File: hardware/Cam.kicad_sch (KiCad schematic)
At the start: 1 part

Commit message: feat(Hw):Update_Schematic_And_BOM
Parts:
- removed Cam1: F31L-1A7H1-11024, Connector_FFC-FPC:Hirose_FH12-24S-0.5SH_1x24-1MP_P0.50mm_Horizontal, symbol F31L-1A7H1-11024:F31L-1A7H1-11024
- added J1: Conn_01x20, Connector_FFC-FPC:Hirose_FH12-20S-0.5SH_1x20-1MP_P0.50mm_Horizontal, symbol Connector_Generic:Conn_01x20
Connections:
- net +3V3: now also J1.19 (Pin_19), J1.20 (Pin_20)
- net CSI_SCK: now also J1.13 (Pin_13)
- net CSI_SDA: now also J1.14 (Pin_14)
- net GND: now also J1.1 (Pin_1), J1.12 (Pin_12), J1.15 (Pin_15), J1.17 (Pin_17), J1.18 (Pin_18), J1.3 (Pin_3), J1.6 (Pin_6), J1.9 (Pin_9)
- net MCSI_CKN: now also J1.8 (Pin_8)
- net MCSI_CKP: now also J1.7 (Pin_7)
- net MCSI_D0N: now also J1.5 (Pin_5)
- net MCSI_D0P: now also J1.4 (Pin_4)
- net MCSI_D1N: now also J1.11 (Pin_11)
- net MCSI_D1P: now also J1.10 (Pin_10)
- net MCSI_MCLK: now also J1.2 (Pin_2)
- net MCSI_RST: now also J1.16 (Pin_16)

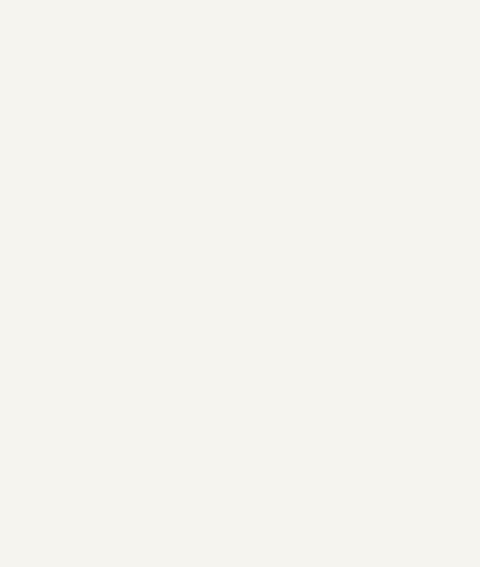
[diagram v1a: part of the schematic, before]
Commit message: feat(Hw):Update_Schematic_And_Floorplan
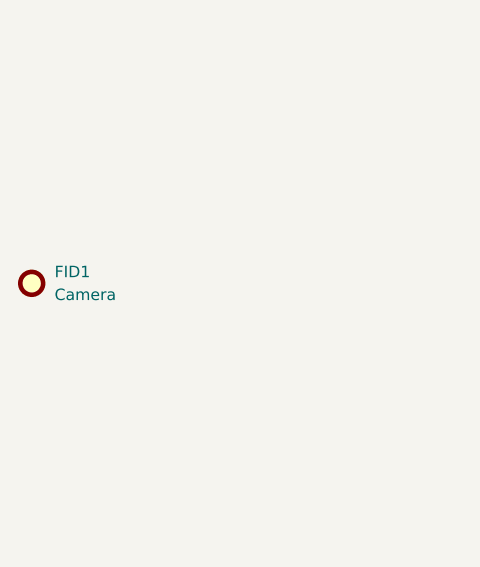
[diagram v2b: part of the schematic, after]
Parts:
- added FID1: Camera, Footprints:Camera, symbol Mechanical:Fiducial
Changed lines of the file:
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@@
+		)
+	)
+	(symbol
+		(lib_id "Mechanical:Fiducial")
+		(at 53.34 54.61 0)
+		(unit 1)
+		(exclude_from_sim no)
+		(in_bom no)
+		(on_board yes)
+		(dnp no)
+		(fields_autoplaced yes)
+		(property "Reference" "FID1"
+			(at 55.88 53.3399 0)
+			(effects
+				(font
+					(size 1.27 1.27)
+				)
+				(justify left)
+			)
+		)
+		(property "Value" "Camera"
+			(at 55.88 55.8799 0)
+			(effects
+				(font
+					(size 1.27 1.27)
+				)
+				(justify left)
+			)
+		)
+		(property "Footprint" "Footprints:Camera"
+			(at 53.34 54.61 0)
+			(effects
+				(font
+					(size 1.27 1.27)
+				)
+				(hide yes)
+			)
+		)
+		(property "Datasheet" "~"
+			(at 53.34 54.61 0)
+			(effects
+				(font
+					(size 1.27 1.27)
+				)
+				(hide yes)
+			)
+		)
+		(property "Description" "Fiducial Marker"
+			(at 53.34 54.61 0)
+			(effects
+				(font
+					(size 1.27 1.27)
+				)
+				(hide yes)
+			)
+		)
+		(property "manf#" "https://www.luckfox.com/EN-SC3336-3MP-Camera-B"
+			(at 53.34 54.61 0)
+			(effects
+				(font
+					(size 1.27 1.27)
+				)
+				(hide yes)
+			)
+		)
+		(instances
+			(project ""
+				(path "/aee06ce3-1da5-4230-bf8f-9d1068f7ddd5/81efd129-08c1-4996-9ee0-a58d47ad59bf"
+					(reference "FID1")
+					(unit 1)
+				)
+			)
 		)
 	)

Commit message: feat(Hw):Update_Schematic_And_Floorplan
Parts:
- FID1: footprint Footprints:Camera -> Footprints:Untitled
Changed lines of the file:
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@@
 			)
 		)
-		(property "Footprint" "Footprints:Camera"
+		(property "Footprint" "Footprints:Untitled"
 			(at 53.34 54.61 0)
 			(effects

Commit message: feat(Hw):Update_Route
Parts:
- added J3: FLEX_TO_CAM, symbol Connector:Conn_01x01_Pin
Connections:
- no-connect marks 0 -> 1
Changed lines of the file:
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@@
 		(color 0 0 0 0)
+	)
+	(no_connect
+		(at 58.42 67.31)
 	)
 	(wire
@@
 					(unit 1)
 				)
+			)
+		)
+	)
+	(symbol
+		(lib_id "Connector:Conn_01x01_Pin")
+		(at 53.34 67.31 0)
+		(unit 1)
+		(exclude_from_sim no)
+		(in_bom yes)
+		(on_board yes)
+		(dnp no)
+		(fields_autoplaced yes)
+		(property "Reference" "J3"
+			(at 53.975 62.23 0)
+			(effects
+				(font
+					(size 1.27 1.27)
+				)
+			)
+		)
+		(property "Value" "FLEX_TO_CAM"
+			(at 53.975 64.77 0)
+			(effects
+				(font
+					(size 1.27 1.27)
+				)
+			)
+		)
+		(property "Footprint" ""
+			(at 53.34 67.31 0)
+			(effects
+				(font
+					(size 1.27 1.27)
+				)
+				(hide yes)
+			)
+		)
+		(property "Datasheet" "~"
+			(at 53.34 67.31 0)
+			(effects
+				(font
+					(size 1.27 1.27)
+				)
+				(hide yes)
+			)
+		)
+		(property "Description" "Generic connector, single row, 01x01, script generated"
+			(at 53.34 67.31 0)
+			(effects
+				(font
+					(size 1.27 1.27)
+				)
+				(hide yes)
+			)
+		)
+		(property "LCSC#" "C22434842"
+			(at 53.34 67.31 0)
+			(effects
+				(font
+					(size 1.27 1.27)
+				)
+				(hide yes)
+			)
+		)
+		(pin "1"
+		)
+		(instances
+			(project "Badge-HackGDL-2026"
+				(path "/aee06ce3-1da5-4230-bf8f-9d1068f7ddd5/81efd129-08c1-4996-9ee0-a58d47ad59bf"
+					(reference "J3")
+					(unit 1)
+				)

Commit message: feat(Hw):Update_Schematic_And_Route
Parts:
- renumbered FID1 to FID?, J1 to J?, J3 to J?
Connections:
- net +3V3: now also J?.1 (Pin_1), J?.2 (Pin_2); no longer J?.19 (Pin_19), J?.20 (Pin_20)
- net CSI_SCK: now also J?.8 (Pin_8); no longer J?.13 (Pin_13)
- net CSI_SDA: now also J?.7 (Pin_7); no longer J?.14 (Pin_14)
- net GND: now also J?.20 (Pin_20), J?.4 (Pin_4); no longer J?.1 (Pin_1), J?.17 (Pin_17)
- net MCSI_CKN: now also J?.13 (Pin_13); no longer J?.8 (Pin_8)
- net MCSI_CKP: now also J?.14 (Pin_14); no longer J?.7 (Pin_7)
- net MCSI_D0N: now also J?.16 (Pin_16); no longer J?.5 (Pin_5)
- net MCSI_D0P: now also J?.17 (Pin_17); no longer J?.4 (Pin_4)
- net MCSI_D1N: now also J?.10 (Pin_10); no longer J?.11 (Pin_11)
- net MCSI_D1P: now also J?.11 (Pin_11); no longer J?.10 (Pin_10)
- net MCSI_MCLK: now also J?.19 (Pin_19); no longer J?.2 (Pin_2)
- net MCSI_RST: now also J?.5 (Pin_5); no longer J?.16 (Pin_16)
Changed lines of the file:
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@@
 	(symbol
 		(lib_id "Connector_Generic:Conn_01x20")
-		(at 157.48 64.77 0)
-		(mirror x)
+		(at 157.48 62.23 0)
 		(unit 1)
 		(exclude_from_sim no)
@@
 		(on_board yes)
 		(dnp no)
-		(property "Reference" "J1"
-			(at 157.48 33.02 0)
+		(property "Reference" "J?"
+			(at 157.48 93.98 0)
 			(effects
 				(font
@@
 		)
 		(property "Value" "Conn_01x20"
-			(at 157.48 35.56 0)
+			(at 157.48 91.44 0)
 			(effects
 				(font
@@
 		)
 		(property "Footprint" "Connector_FFC-FPC:Hirose_FH12-20S-0.5SH_1x20-1MP_P0.50mm_Horizontal"
-			(at 157.48 64.77 0)
+			(at 157.48 62.23 0)
 			(effects
 				(font
@@
 		)
 		(property "Datasheet" "~"
-			(at 157.48 64.77 0)
+			(at 157.48 62.23 0)
 			(effects
 				(font
@@
 		)
 		(property "Description" "Generic connector, single row, 01x20, script generated (kicad-library-utils/schlib/autogen/connector/)"
-			(at 157.48 64.77 0)
+			(at 157.48 62.23 0)
 			(effects
 				(font
@@
 		)
 		(property "Mnfr#" ""
-			(at 157.48 64.77 0)
+			(at 157.48 62.23 0)
 			(effects
 				(font
@@
 		)
 		(property "SNAPEDA_PN" ""
-			(at 157.48 64.77 0)
+			(at 157.48 62.23 0)
 			(effects
 				(font
@@
 		)
 		(instances
+			(project "Cam"
+				(path "/4f679915-e6d1-4835-bbdc-b9d0e7615f17"
+					(reference "J?")
+					(unit 1)
+				)
+			)
 			(project ""
 				(path "/aee06ce3-1da5-4230-bf8f-9d1068f7ddd5/81efd129-08c1-4996-9ee0-a58d47ad59bf"
@@
 		(dnp no)
 		(fields_autoplaced yes)
-		(property "Reference" "J3"
+		(property "Reference" "J?"
 			(at 53.975 62.23 0)
 			(effects
@@
 		)
 		(instances
+			(project "Cam"
+				(path "/4f679915-e6d1-4835-bbdc-b9d0e7615f17"
+					(reference "J?")
+					(unit 1)
+				)
+			)
 			(project "Badge-HackGDL-2026"
 				(path "/aee06ce3-1da5-4230-bf8f-9d1068f7ddd5/81efd129-08c1-4996-9ee0-a58d47ad59bf"
@@
 		(on_board yes)
 		(dnp no)
-		(property "Reference" "#PWR0125"
+		(property "Reference" "#PWR?"
 			(at 137.16 36.83 0)
 			(effects
@@
 		)
 		(instances
+			(project "Cam"
+				(path "/4f679915-e6d1-4835-bbdc-b9d0e7615f17"
+					(reference "#PWR?")
+					(unit 1)
+				)
+			)
 			(project "Badge-HackGDL-2026"
 				(path "/aee06ce3-1da5-4230-bf8f-9d1068f7ddd5/81efd129-08c1-4996-9ee0-a58d47ad59bf"
@@
 		(on_board yes)
 		(dnp no)
-		(property "Reference" "#PWR09"
+		(property "Reference" "#PWR?"
 			(at 137.16 97.79 0)
 			(effects
@@
 		)
 		(instances
+			(project "Cam"
+				(path "/4f679915-e6d1-4835-bbdc-b9d0e7615f17"
+					(reference "#PWR?")
+					(unit 1)
+				)
+			)
 			(project "Badge-HackGDL-2026"
 				(path "/aee06ce3-1da5-4230-bf8f-9d1068f7ddd5/81efd129-08c1-4996-9ee0-a58d47ad59bf"
@@
 		(dnp no)
 		(fields_autoplaced yes)
-		(property "Reference" "FID1"
+		(property "Reference" "FID?"
 			(at 55.88 53.3399 0)
 			(effects
@@
 		)
 		(instances
+			(project "Cam"
+				(path "/4f679915-e6d1-4835-bbdc-b9d0e7615f17"
+					(reference "FID?")
+					(unit 1)
+				)
+			)
 			(project ""
 				(path "/aee06ce3-1da5-4230-bf8f-9d1068f7ddd5/81efd129-08c1-4996-9ee0-a58d47ad59bf"
@@
 		)
 	)
+	(sheet_instances
+		(path "/"
+			(page "1")
+		)
+	)
+	(embedded_fonts no)
 )

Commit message: feat(Hw):Update_Schematic_And_Route
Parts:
- gave numbers to parts that had none: 3
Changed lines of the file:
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@@
-	(wire
-		(pts
-			(xy 132.08 39.37) (xy 137.16 39.37)
-		)
-		(stroke
-			(width 0)
-			(type default)
-		)
-	)
 	(wire
 		(pts
@@
 		(pts
 			(xy 151.13 49.53) (xy 152.4 49.53)
+		)
+		(stroke
+			(width 0)
+			(type default)
+		)
+	)
+	(wire
+		(pts
+			(xy 133.35 39.37) (xy 137.16 39.37)
 		)
 		(stroke
@@
 		)
 	)
+	(hierarchical_label "+3.3v"
+		(shape input)
+		(at 133.35 39.37 180)
+		(effects
+			(font
+				(size 1.27 1.27)
+			)
+			(justify right)
+		)
+	)
 	(hierarchical_label "MCSI_D0N"
 		(shape output)
@@
 		(shape input)
 		(at 151.13 85.09 180)
-		(effects
-			(font
-				(size 1.27 1.27)
-			)
-			(justify right)
-		)
-	)
-	(hierarchical_label "v_3v3"
-		(shape output)
-		(at 132.08 39.37 180)
 		(effects
 			(font
@@
 		(on_board yes)
 		(dnp no)
-		(property "Reference" "J?"
+		(property "Reference" "J1"
 			(at 157.48 93.98 0)
 			(effects
@@
 		(dnp no)
 		(fields_autoplaced yes)
-		(property "Reference" "J?"
+		(property "Reference" "J3"
 			(at 53.975 62.23 0)
 			(effects
@@
 		(on_board yes)
 		(dnp no)
-		(property "Reference" "#PWR?"
+		(property "Reference" "#PWR0125"
 			(at 137.16 36.83 0)
 			(effects
@@
 		(on_board yes)
 		(dnp no)
-		(property "Reference" "#PWR?"
+		(property "Reference" "#PWR09"
 			(at 137.16 97.79 0)
 			(effects
@@
 		(dnp no)
 		(fields_autoplaced yes)
-		(property "Reference" "FID?"
+		(property "Reference" "FID1"
 			(at 55.88 53.3399 0)
 			(effects

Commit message: feat(Hw):Update_Route
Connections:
- net +3V3 renamed +3.3v
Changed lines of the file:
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@@
-	(wire
-		(pts
-			(xy 137.16 33.02) (xy 137.16 39.37)
-		)
-		(stroke
-			(width 0)
-			(type default)
-		)
-	)
 	(wire
 		(pts
@@
 					(unit 1)
 				)
-			)
-		)
-	)
-	(symbol
-		(lib_id "power:+3V3")
-		(at 137.16 33.02 0)
-		(unit 1)
-		(exclude_from_sim no)
-		(in_bom yes)
-		(on_board yes)
-		(dnp no)
-		(property "Reference" "#PWR0125"
-			(at 137.16 36.83 0)
-			(effects
-				(font
-					(size 1.27 1.27)
-				)
-				(hide yes)
-			)
-		)
-		(property "Value" "+3V3"
-			(at 139.954 33.02 0)
-			(effects
-				(font
-					(size 1.27 1.27)
-				)
-			)
-		)
-		(property "Footprint" ""
-			(at 137.16 33.02 0)
-			(effects
-				(font
-					(size 1.27 1.27)
-				)
-				(hide yes)
-			)
-		)
-		(property "Datasheet" ""
-			(at 137.16 33.02 0)
-			(effects
-				(font
-					(size 1.27 1.27)
-				)
-				(hide yes)
-			)
-		)
-		(property "Description" "Power symbol creates a global label with name \"+3V3\""
-			(at 137.16 33.02 0)
-			(effects
-				(font
-					(size 1.27 1.27)
-				)
-				(hide yes)
-			)
-		)
-		(pin "1"
-		)
-		(instances
-			(project "Cam"
-				(path "/4f679915-e6d1-4835-bbdc-b9d0e7615f17"
-					(reference "#PWR?")
-					(unit 1)
-				)
-			)
-			(project "Badge-HackGDL-2026"
-				(path "/aee06ce3-1da5-4230-bf8f-9d1068f7ddd5/81efd129-08c1-4996-9ee0-a58d47ad59bf"
-					(reference "#PWR0125")
-					(unit 1)
-				)

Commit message: feat(Hw):Update_3Dmodels_And_Rear_Board
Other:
- company: (none) -> Electronic Cats
- title: (none) -> Badge-HackGDL-2026
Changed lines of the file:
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@@
 	(generator_version "9.0")
 	(paper "A5")
+	(title_block
+		(title "Badge-HackGDL-2026")
+		(date "2026-01-15")
+		(rev "v1.0")
+		(company "Electronic Cats")
+		(comment 1 "Lizeth Gallegos Martínez")
+	)
 	(text "CAM"
 		(exclude_from_sim no)
